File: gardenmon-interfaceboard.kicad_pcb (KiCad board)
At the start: 2 copper layers, 10 parts, among them J1 Conn_02x20_Odd_Even, J2 Conn_01x04, J3 Conn_01x10, J4 Conn_01x04, J5 Conn_01x04, J6 Conn_01x03

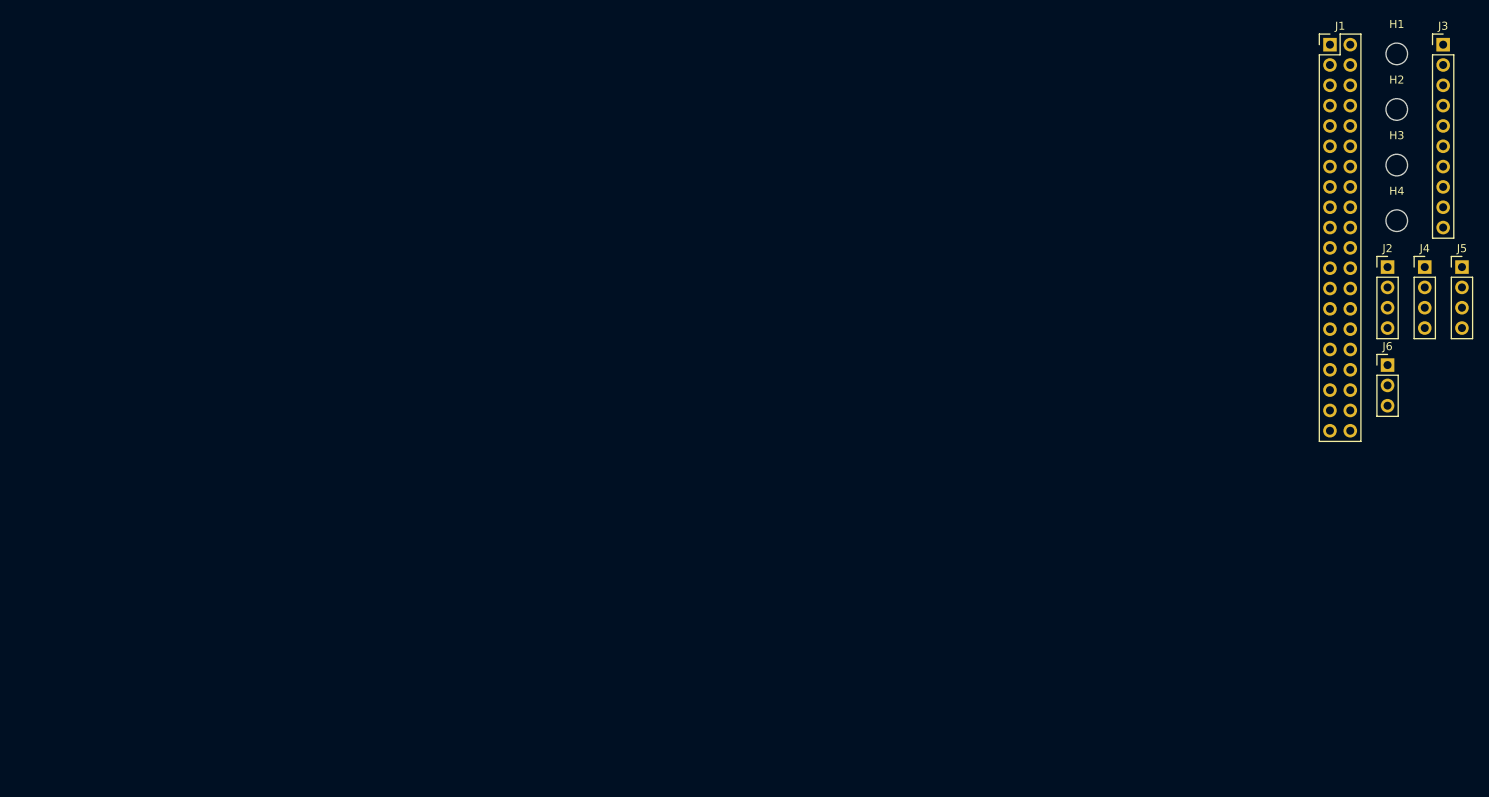
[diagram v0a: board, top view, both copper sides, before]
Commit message: pcb: add footprints, board layout
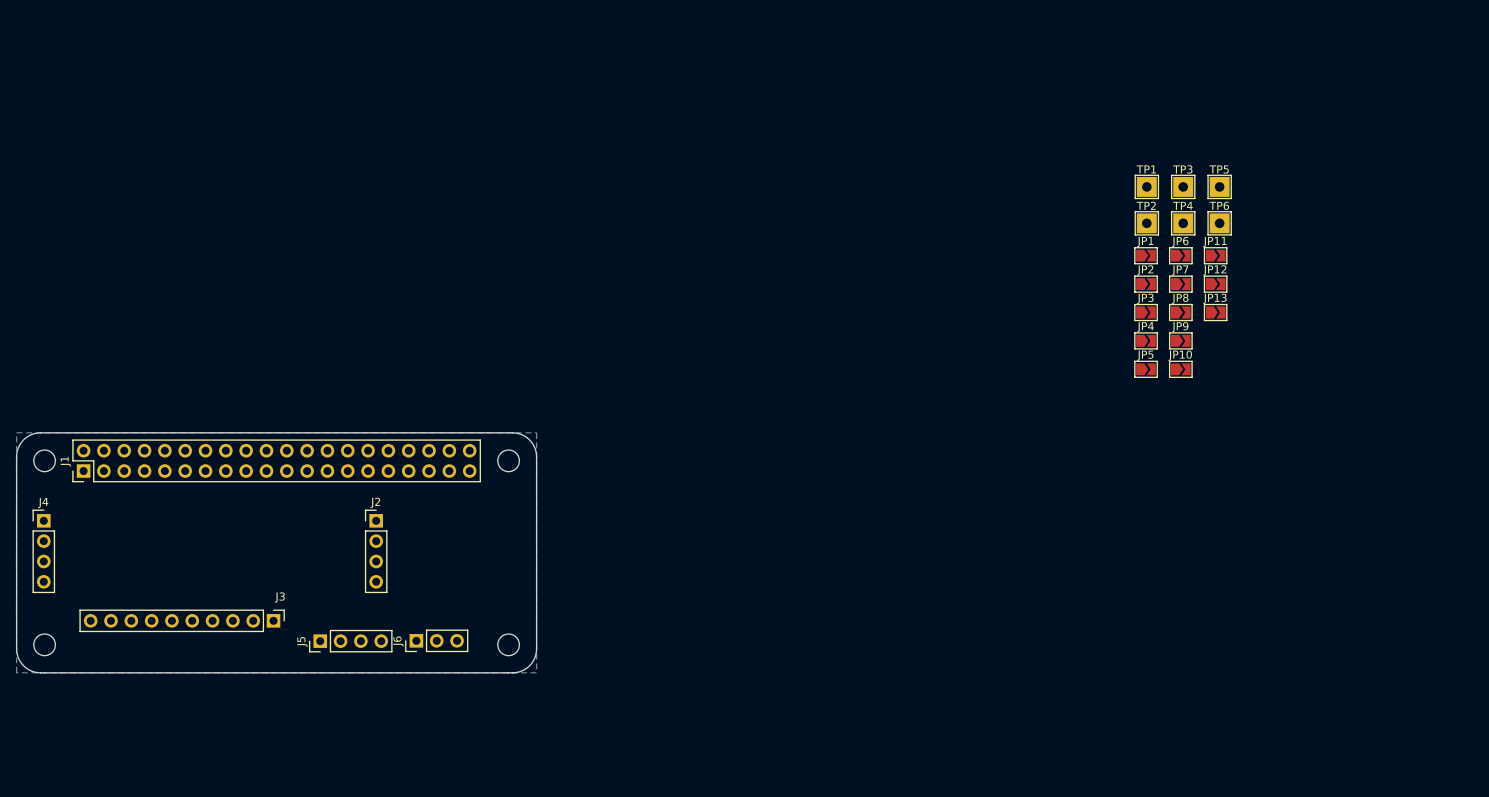
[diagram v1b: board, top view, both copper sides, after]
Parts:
- added JP1: SolderJumper_2_Bridged, Jumper:SolderJumper-2_P1.3mm_Open_TrianglePad1.0x1.5mm, F.Cu at (237.2, 56.9)
- added JP10: SolderJumper_2_Bridged, Jumper:SolderJumper-2_P1.3mm_Open_TrianglePad1.0x1.5mm, F.Cu at (241.5, 71.1)
- added JP11: SolderJumper_2_Bridged, Jumper:SolderJumper-2_P1.3mm_Open_TrianglePad1.0x1.5mm, F.Cu at (245.9, 56.9)
- added JP12: SolderJumper_2_Bridged, Jumper:SolderJumper-2_P1.3mm_Open_TrianglePad1.0x1.5mm, F.Cu at (245.9, 60.4)
- added JP13: SolderJumper_2_Bridged, Jumper:SolderJumper-2_P1.3mm_Open_TrianglePad1.0x1.5mm, F.Cu at (245.9, 64.0)
- added JP2: SolderJumper_2_Bridged, Jumper:SolderJumper-2_P1.3mm_Open_TrianglePad1.0x1.5mm, F.Cu at (237.2, 60.4)
- added JP3: SolderJumper_2_Bridged, Jumper:SolderJumper-2_P1.3mm_Open_TrianglePad1.0x1.5mm, F.Cu at (237.2, 64.0)
- added JP4: SolderJumper_2_Bridged, Jumper:SolderJumper-2_P1.3mm_Open_TrianglePad1.0x1.5mm, F.Cu at (237.2, 67.5)
- added JP5: SolderJumper_2_Bridged, Jumper:SolderJumper-2_P1.3mm_Open_TrianglePad1.0x1.5mm, F.Cu at (237.2, 71.1)
- added JP6: SolderJumper_2_Bridged, Jumper:SolderJumper-2_P1.3mm_Open_TrianglePad1.0x1.5mm, F.Cu at (241.5, 56.9)
- added JP7: SolderJumper_2_Bridged, Jumper:SolderJumper-2_P1.3mm_Open_TrianglePad1.0x1.5mm, F.Cu at (241.5, 60.4)
- added JP8: SolderJumper_2_Bridged, Jumper:SolderJumper-2_P1.3mm_Open_TrianglePad1.0x1.5mm, F.Cu at (241.5, 64.0)
- added JP9: SolderJumper_2_Bridged, Jumper:SolderJumper-2_P1.3mm_Open_TrianglePad1.0x1.5mm, F.Cu at (241.5, 67.5)
- added TP1: TestPoint, TestPoint:TestPoint_THTPad_2.5x2.5mm_Drill1.2mm, F.Cu at (237.3, 48.3)
- added TP2: TestPoint, TestPoint:TestPoint_THTPad_2.5x2.5mm_Drill1.2mm, F.Cu at (237.3, 52.8)
- added TP3: TestPoint, TestPoint:TestPoint_THTPad_2.5x2.5mm_Drill1.2mm, F.Cu at (241.8, 48.3)
- added TP4: TestPoint, TestPoint:TestPoint_THTPad_2.5x2.5mm_Drill1.2mm, F.Cu at (241.8, 52.8)
- added TP5: TestPoint, TestPoint:TestPoint_THTPad_2.5x2.5mm_Drill1.2mm, F.Cu at (246.4, 48.3)
- added TP6: TestPoint, TestPoint:TestPoint_THTPad_2.5x2.5mm_Drill1.2mm, F.Cu at (246.4, 52.8)
- moved H2 181.8 mm to (99.5, 105.5)
- moved H1 176.5 mm to (99.5, 82.5)
- moved J4 175.5 mm to (99.4, 90.0)
- moved J1 164.7 mm to (104.4, 83.8), turned to 90 degrees
- moved J3 163.0 mm to (128.1, 102.5), turned to -90 degrees
- moved J5 150.2 mm to (134.0, 105.0), turned to 90 degrees
- moved J2 130.3 mm to (140.9, 90.0)
- moved J6 126.2 mm to (146.0, 105.0), turned to 90 degrees
- moved H3 126.2 mm to (157.5, 105.5)
- moved H4 115.0 mm to (157.5, 82.5)
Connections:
- J2 pad 1: +3V3 -> Net-(J2-Pin_1)
- J2 pad 4: /smoist_sig -> /sms_sig_probe
- J3 pad 1: +3V3 -> Net-(J3-Pin_1)
- J3 pad 3: /i2c_scl -> /i2c_scl_ads1115
- J3 pad 4: /i2c_sda -> /i2c_sda_ads1115
- J3 pad 7: /smoist_sig -> /sms_sig
- J4 pad 1: +3V3 -> Net-(J4-Pin_1)
- J4 pad 3: /i2c_scl -> /i2c_scl_sht30
- J4 pad 4: /i2c_sda -> /i2c_sda_sht30
- J5 pad 1: +3V3 -> Net-(J5-Pin_1)
- J5 pad 3: /i2c_scl -> /i2c_scl_als
- J5 pad 4: /i2c_sda -> /i2c_sda_als
- J6 pad 1: +3V3 -> Net-(J6-Pin_1)
- J6 pad 2: /1wire_data -> /1wire_data_ds18b20
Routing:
- added copper zone on B.Cu, net GND
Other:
- board outline added: 65 x 30 mm
- board text added: "ADS1115"
- board text added: "Case"
- board text added: "SMS INTERFACE BOARD"

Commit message: rev0: release of rev0
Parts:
- removed the J3 at (128.1, 102.5)
- added C1: 10uF, Capacitor_SMD:C_0603_1608Metric_Pad1.08x0.95mm_HandSolder, F.Cu at (121.5, 106.0)
- added C2: 0.1uF, Capacitor_SMD:C_0603_1608Metric_Pad1.08x0.95mm_HandSolder, F.Cu at (123.5, 106.0)
- added G***: LOGO, LOGO, F.Cu at (127.0, 62.0)
- added R1: 10k, Resistor_SMD:R_0603_1608Metric_Pad0.98x0.95mm_HandSolder, F.Cu at (121.0, 114.0)
- added R2: 4.7k, Resistor_SMD:R_0603_1608Metric_Pad0.98x0.95mm_HandSolder, F.Cu at (120.5, 84.0)
- added U1: MCP3221A5, Package_TO_SOT_SMD:SOT-23-5_HandSoldering, F.Cu at (127.5, 106.0)
- J2: renamed from J4; footprint Connector_PinHeader_2.54mm:PinHeader_1x04_P2.54mm_Vertical -> Connector_JST:JST_PH_S4B-PH-K_1x04_P2.00mm_Horizontal
- J3: renamed from J5; footprint Connector_PinHeader_2.54mm:PinHeader_1x04_P2.54mm_Vertical -> Connector_JST:JST_PH_S4B-PH-K_1x04_P2.00mm_Horizontal
- J4: renamed from J2; value Conn_01x04 -> Conn_01x02; footprint Connector_PinHeader_2.54mm:PinHeader_1x04_P2.54mm_Vertical -> Connector_JST:JST_PH_S2B-PH-K_1x02_P2.00mm_Horizontal
- J5: renamed from J6; footprint Connector_PinHeader_2.54mm:PinHeader_1x03_P2.54mm_Vertical -> Connector_JST:JST_PH_S3B-PH-K_1x03_P2.00mm_Horizontal
- moved TP5 143.4 mm to (117.5, 115.8)
- moved TP4 142.9 mm to (122.5, 119.5)
- moved TP6 132.4 mm to (125.0, 115.0)
- moved JP8 126.8 mm to (120.5, 79.0), turned to -90 degrees
- moved JP5 126.1 mm to (121.8, 96.5), turned to 180 degrees
- moved JP7 126.0 mm to (123.5, 111.2), turned to 90 degrees
- moved JP4 125.7 mm to (121.5, 75.0), turned to 180 degrees
- moved JP1 124.2 mm to (121.8, 93.5), turned to 180 degrees
- moved JP9 124.0 mm to (123.5, 83.8), turned to 180 degrees
- moved TP3 122.9 mm to (125.5, 88.0)
- moved JP2 122.7 mm to (121.8, 90.5), turned to 180 degrees
- moved JP11 121.8 mm to (126.5, 111.2), turned to -90 degrees
- moved JP6 120.0 mm to (121.5, 69.0), turned to 180 degrees
- moved JP3 120.0 mm to (121.5, 72.0), turned to 180 degrees
- moved JP10 119.0 mm to (124.0, 100.7), turned to -90 degrees
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- renumbered JP7 to JP1, JP3 to JP10, JP2 to JP11, JP4 to JP12, JP5 to JP13, JP8 to JP2, JP10 to JP3, JP11 to JP4, JP6 to JP5, JP9 to JP6, JP1 to JP7, JP12 to JP8, JP13 to JP9, TP5 to TP4, TP6 to TP5, TP4 to TP6
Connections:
- J1 pad 1: +3.3V -> +3V3
- J1 pad 17: +3.3V -> unconnected-(J1-Pin_17-Pad17)
- J4 pad 1: Net-(J2-Pin_1) (its old number) -> Net-(J4-Pin_1)
- J4 pad 2: GND -> Net-(J4-Pin_2)
- JP11 pad 1: /sms_sig -> Net-(JP11-A)
- JP11 pad 2: /sms_sig_probe -> Net-(J4-Pin_2)
- JP12 pad 2: /i2c_scl_ads1115 -> /i2c_scl_mcp3221
- JP13 pad 2: /i2c_sda_ads1115 -> /i2c_sda_mcp3221
- JP7 pad 1: +3V3 -> Net-(J4-Pin_1)
- JP7 pad 2: Net-(J2-Pin_1) (its old number) -> +3V3
- JP9 pad 1: /i2c_sda -> /1wire_data
- TP4 pad 1: +3.3V -> +3V3
- TP6 pad 1: /sms_sig_probe -> Net-(J4-Pin_2)
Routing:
- net +3V3: track 0.00 -> 120.5 mm
- net /i2c_sda: track 0.00 -> 54.5 mm, vias 0 -> 4
- net /i2c_scl: track 0.00 -> 48.6 mm
- net /1wire_data: track 0.00 -> 22.8 mm, vias 0 -> 2
- net /i2c_sda_sht30: track 0.00 -> 17.3 mm
- net /i2c_scl_sht30: track 0.00 -> 13.6 mm
- net Net-(J4-Pin_2): track 0.00 -> 13.3 mm
- net Net-(JP10-B): track 0.00 -> 9.18 mm
- net Net-(J4-Pin_1): track 0.00 -> 7.72 mm
- net /i2c_sda_mcp3221: track 0.00 -> 7.09 mm
- net /1wire_data_ds18b20: track 0.00 -> 6.34 mm
- net Net-(J5-Pin_1): track 0.00 -> 6.30 mm
- net GND: track 0.00 -> 6.12 mm, vias 0 -> 4
- net /i2c_scl_mcp3221: track 0.00 -> 4.37 mm
- net /i2c_scl_als: track 0.00 -> 4.24 mm
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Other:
- board size 65 x 30 mm -> 30 x 65 mm
- board text added: "+3V3"
- board text added: "1WIRE DATA"
- board text added: "ALS"
- board text added: "ATHS"
- board text added: "GND"
- board text added: "GardenMon Interface Board Rev0"
- board text added: "I2C SCL"
- board text added: "I2C SDA"
- board text added: "SMS"
- board text added: "SMS SIG"
- board text added: "STS"
- board text removed: "ADS1115"
- board text removed: "SMS INTERFACE BOARD"
